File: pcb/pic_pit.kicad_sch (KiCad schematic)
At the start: 19 parts, among them J15 PC SPK, J17 IOout, U10 8259A-2, U23 74LS573, U9 8254

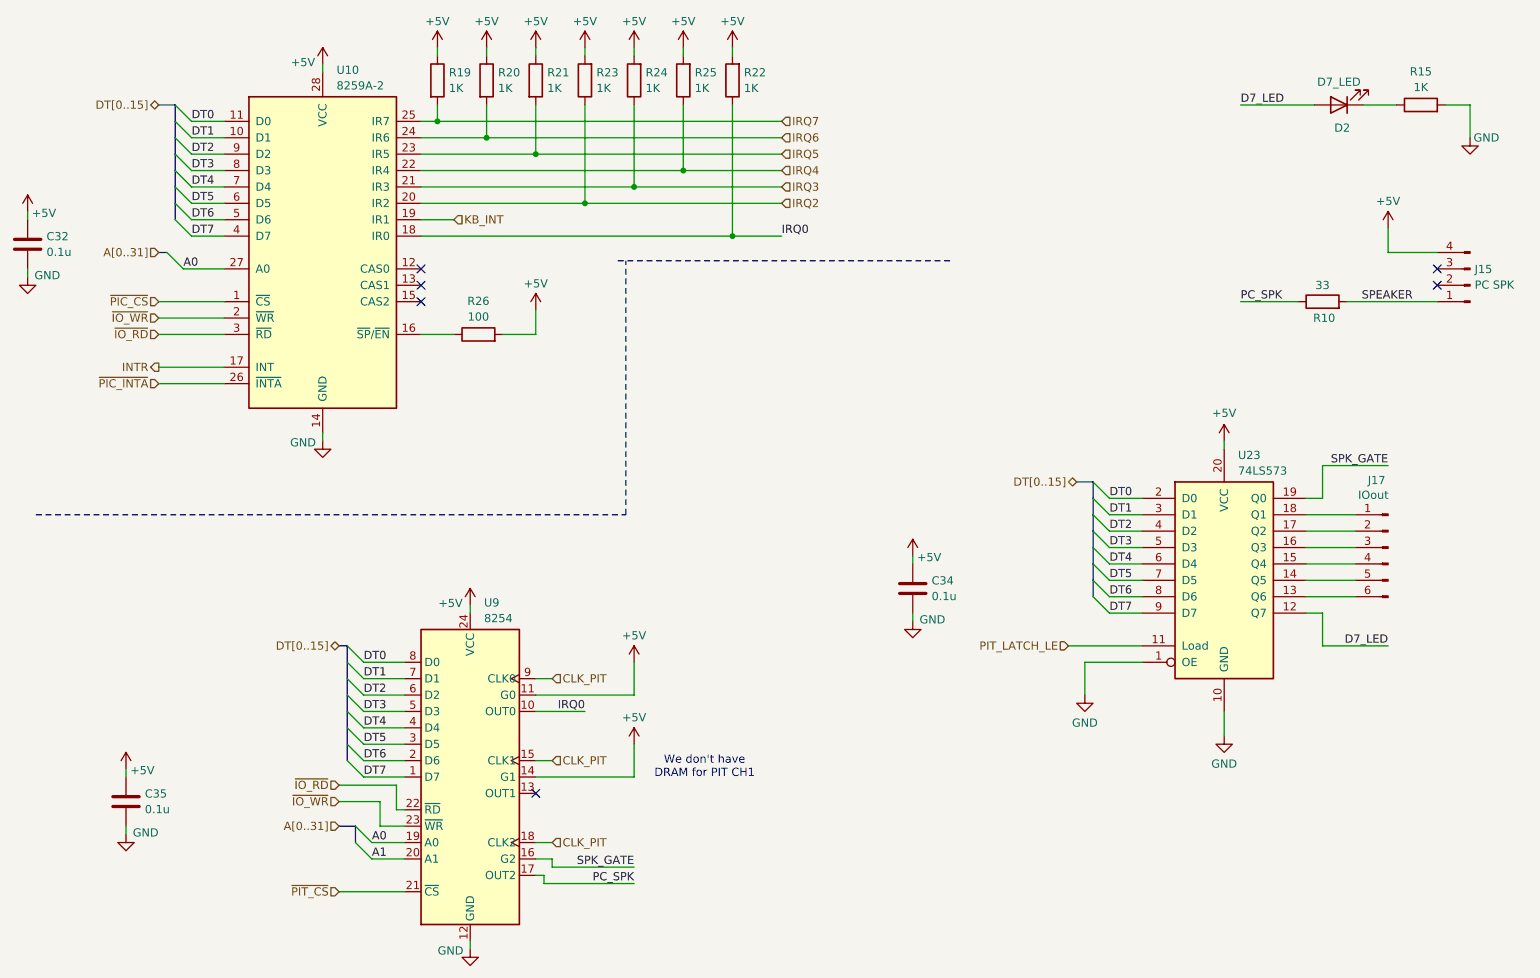
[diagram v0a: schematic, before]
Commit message: updating diagram and pcb to removed U23, driving PIT gate2 directly by PIT_SPK_GATE (former PIT_LATCH_LE), 635 VIAs
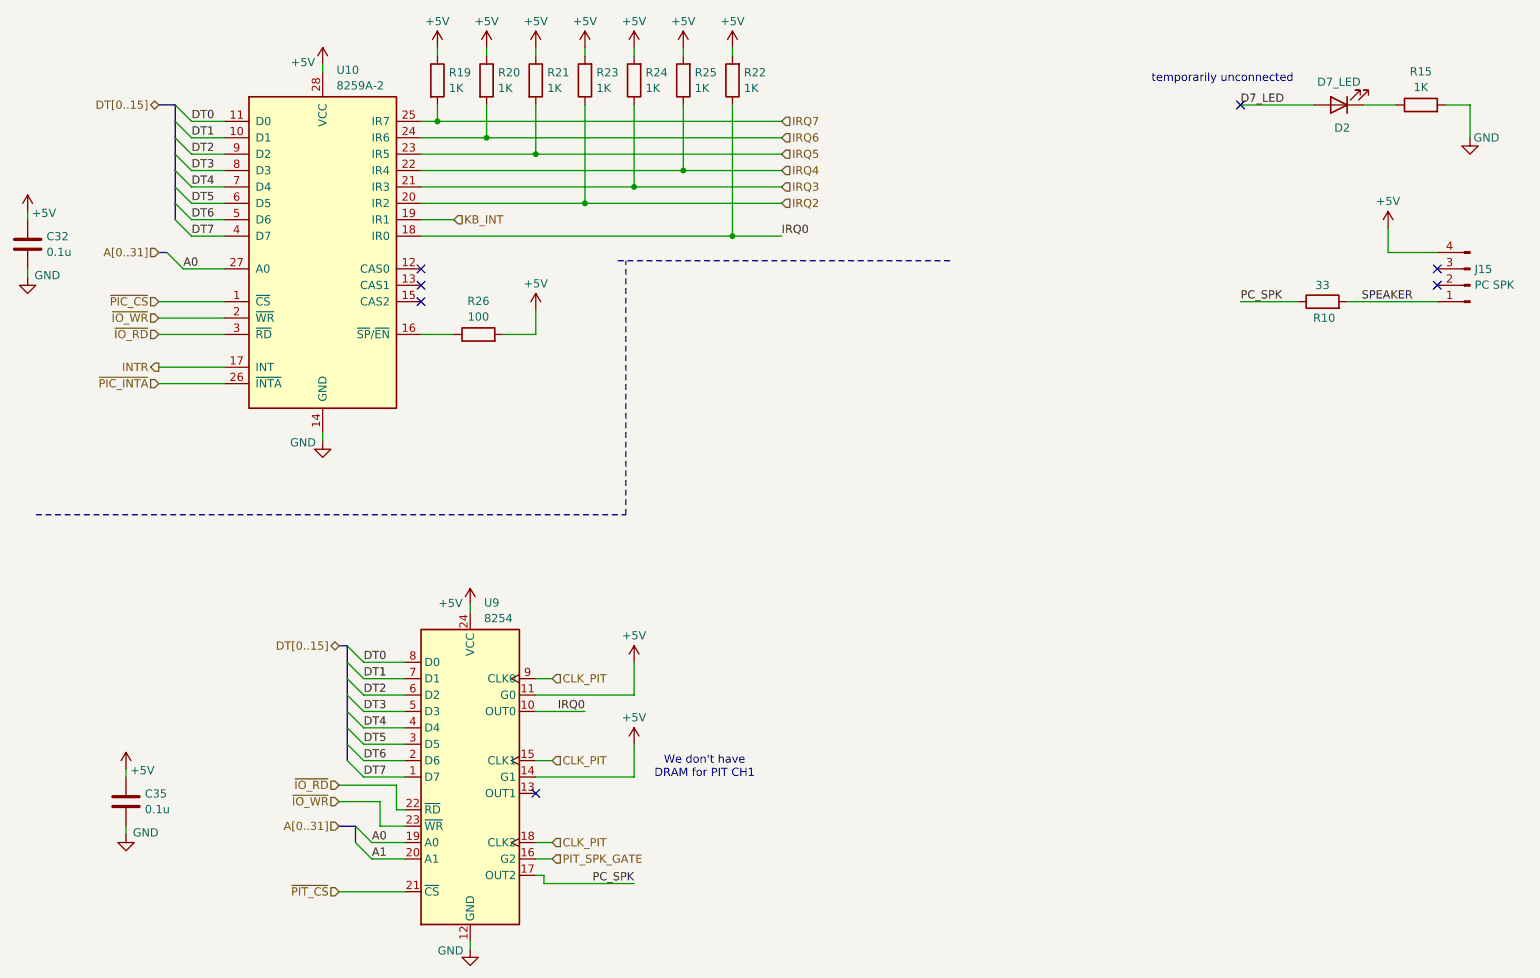
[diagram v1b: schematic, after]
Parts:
- removed C34: 0.1u, Capacitor_SMD:C_0805_2012Metric_Pad1.18x1.45mm_HandSolder, symbol Device:C
- removed J17: IOout, Connector_PinHeader_2.54mm:PinHeader_1x06_P2.54mm_Vertical, symbol Connector:Conn_01x06_Pin
- removed U23: 74LS573, Package_SO:SOP-20_7.5x12.8mm_P1.27mm, symbol 74xx:74LS573
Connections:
- net SPK_GATE renamed PIT_SPK_GATE
- no-connect marks 6 -> 7
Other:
- note added: "temporarily unconnected"

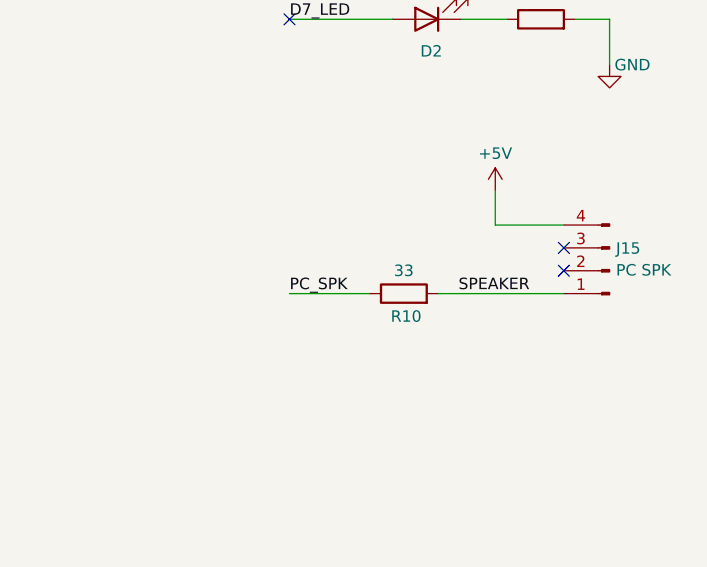
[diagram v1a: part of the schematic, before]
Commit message: reshuffled data order in upper word of ram U13 U14 U17 U18 for easier layout
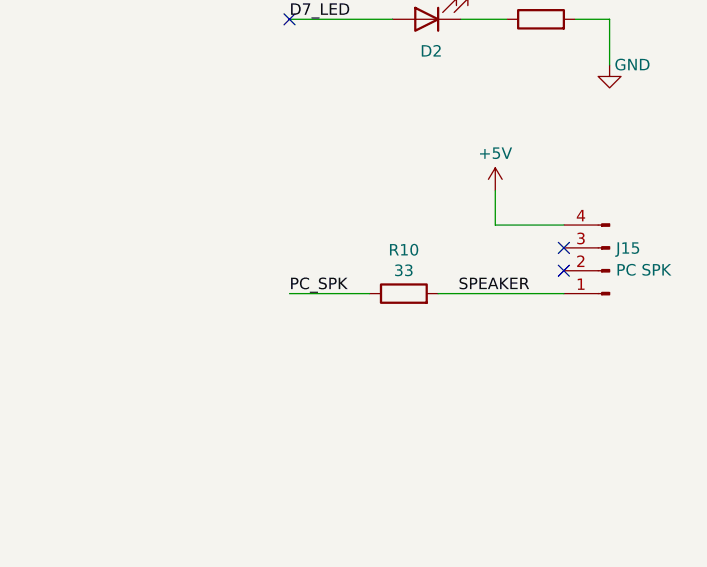
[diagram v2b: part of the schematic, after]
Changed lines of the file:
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@@
 		(dnp no)
 		(property "Reference" "R10"
-			(at 223.774 71.12 90)
+			(at 223.52 63.754 90)
 			(effects
 				(font
